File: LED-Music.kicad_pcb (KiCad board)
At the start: 2 copper layers, 38.1 x 72.4 mm, 34 parts, among them J1 12V 6A, J2 3.5mm Audio Jack, J3 LED, J4 A1-5, J5 PRGRM, J6 D4-8, Q1 GRN-NCH, Q2 RED-NCH, Q3 BLU-NCH, Y1 16MHz

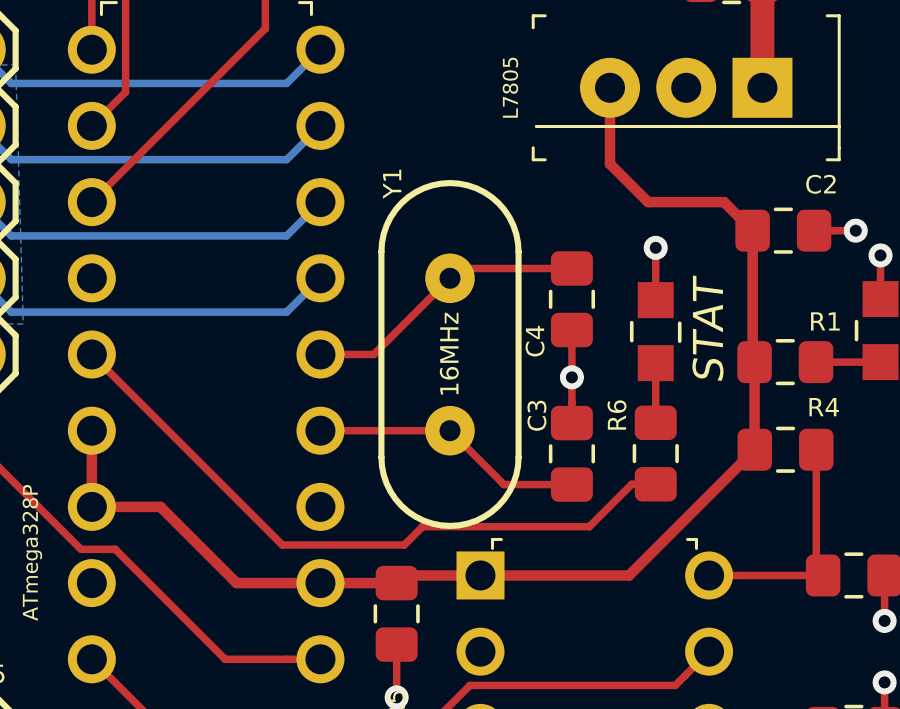
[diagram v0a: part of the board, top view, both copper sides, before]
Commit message: IMP: Update to KiCAD 8.0 File Formats
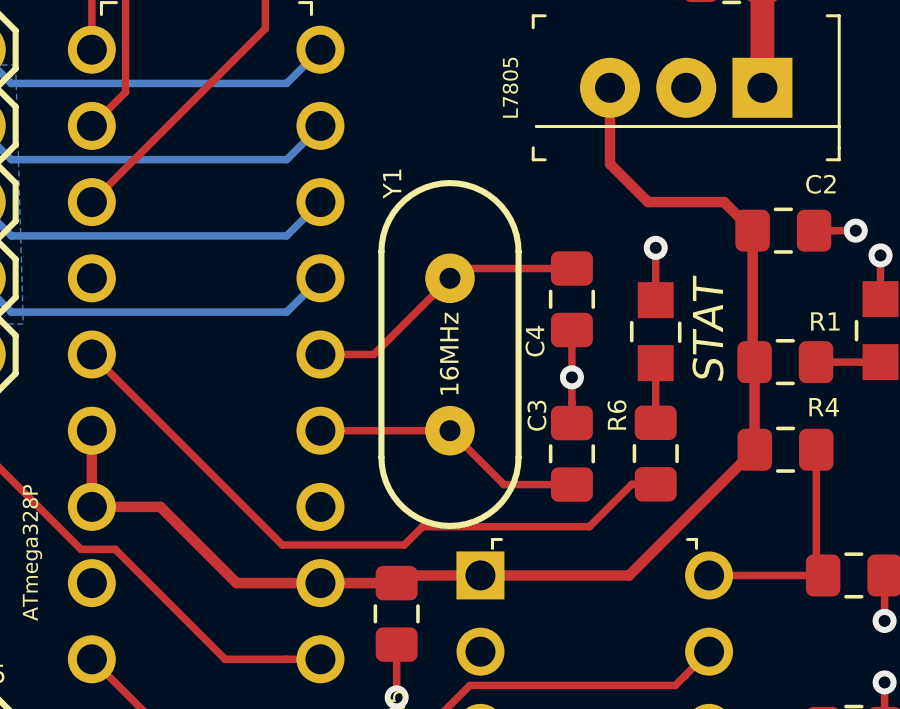
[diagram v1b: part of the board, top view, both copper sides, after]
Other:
- net class 12V removed
- net class Default removed
